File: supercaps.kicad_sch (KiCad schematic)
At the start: 17 parts, among them J7 XT30_F, J8 XT30_F, Q10 Q_PNP_BCE, Q9 Q_NPN_BCE, U17 TLV9301xDBV

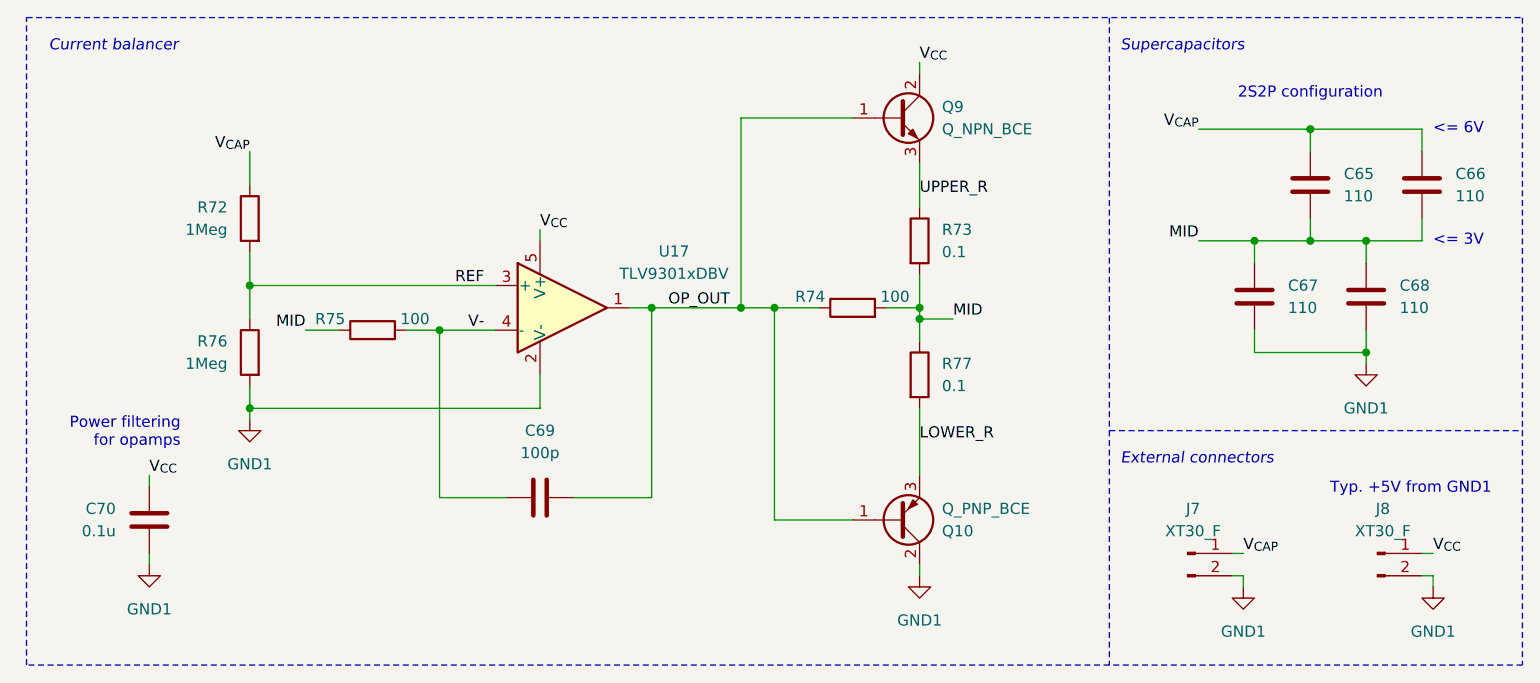
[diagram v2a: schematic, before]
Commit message: Selected BJTs for the supercap balancing circuitry
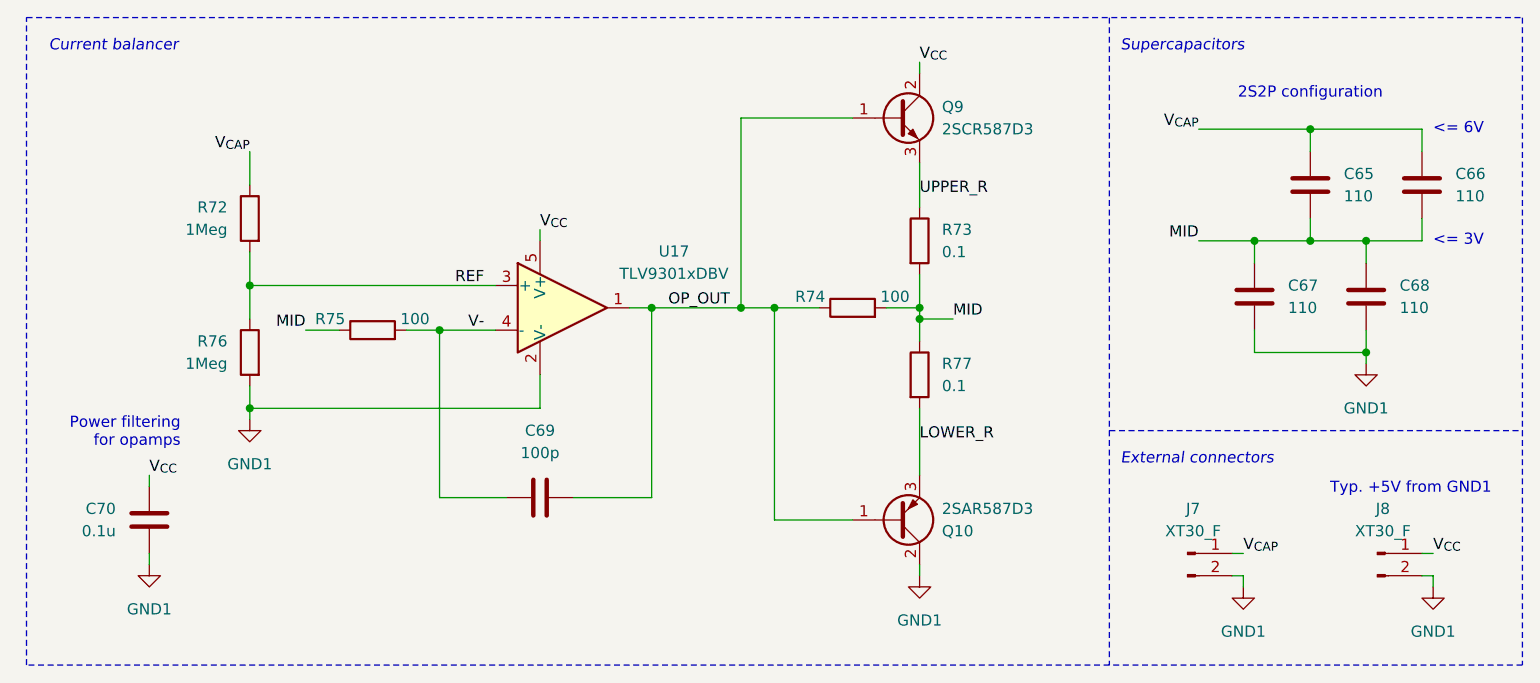
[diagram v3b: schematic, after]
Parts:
- Q10: value Q_PNP_BCE -> 2SAR587D3; footprint (none) -> Package_TO_SOT_SMD:TO-252-2; Mouser Part Number (none) -> 755-2SAR587D3FRATL
- Q9: value Q_NPN_BCE -> 2SCR587D3; footprint (none) -> Package_TO_SOT_SMD:TO-252-2; Mouser Part Number (none) -> 755-2SCR587D3FRATL
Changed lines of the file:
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@@
 			)
 		)
-		(property "Value" "Q_NPN_BCE"
+		(property "Value" "2SCR587D3"
 			(at 125.73 38.0999 0)
 			(effects
@@
 			)
 		)
-		(property "Footprint" ""
+		(property "Footprint" "Package_TO_SOT_SMD:TO-252-2"
 			(at 125.73 34.29 0)
 			(effects
@@
 			)
 		)
-		(property "Datasheet" "~"
+		(property "Datasheet" "https://fscdn.rohm.com/en/products/databook/datasheet/discrete/transistor/bipolar/2scr587d3fratl-e.pdf"
 			(at 120.65 36.83 0)
 			(effects
@@
 		)
 		(property "Description" "NPN transistor, base/collector/emitter"
+			(at 120.65 36.83 0)
+			(effects
+				(font
+					(size 1.27 1.27)
+				)
+				(hide yes)
+			)
+		)
+		(property "Mouser Part Number" "755-2SCR587D3FRATL"
 			(at 120.65 36.83 0)
 			(effects
@@
 			)
 		)
-		(property "Value" "Q_PNP_BCE"
+		(property "Value" "2SAR587D3"
 			(at 125.73 81.2801 0)
 			(effects
@@
 			)
 		)
-		(property "Footprint" ""
+		(property "Footprint" "Package_TO_SOT_SMD:TO-252-2"
 			(at 125.73 85.09 0)
 			(effects
@@
 			)
 		)
-		(property "Datasheet" "~"
+		(property "Datasheet" "https://fscdn.rohm.com/en/products/databook/datasheet/discrete/transistor/bipolar/2sar587d3fratl-e.pdf"
 			(at 120.65 82.55 0)
 			(effects
@@
 			(at 120.65 82.55 0)
 			(effects
+				(font
+					(size 1.27 1.27)
+				)
+				(hide yes)
+			)
+		)
+		(property "Mouser Part Number" "755-2SAR587D3FRATL"
+			(at 120.65 82.55 0)
+			(effects

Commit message: Adjusted some things + changed discharge to have a smaller time constant
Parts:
- R72, R76: Mouser Part Number (none) -> 603-RC0603FR-1010ML
- U17: Mouser Part Number (none) -> 595-TLV9301IDBVR
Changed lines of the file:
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@@
+			)
+		)
+		(property "Mouser Part Number" "595-TLV9301IDBVR"
+			(at 82.55 58.42 0)
+			(effects
+				(font
+					(size 1.27 1.27)
+				)
+				(hide yes)
 			)
 		)
@@
 			)
 		)
-		(property "Datasheet" "~"
+		(property "Datasheet" "https://www.mouser.com/datasheet/2/447/PYu_RC_Group_51_RoHS_L_11-1984063.pdf"
 			(at 46.99 48.26 0)
 			(effects
@@
 		)
 		(property "Description" "Resistor"
+			(at 46.99 48.26 0)
+			(effects
+				(font
+					(size 1.27 1.27)
+				)
+				(hide yes)
+			)
+		)
+		(property "Mouser Part Number" "603-RC0603FR-1010ML"
 			(at 46.99 48.26 0)
 			(effects
@@
 			)
 		)
-		(property "Datasheet" "~"
+		(property "Datasheet" "https://www.mouser.com/datasheet/2/447/PYu_RC_Group_51_RoHS_L_11-1984063.pdf"
 			(at 46.99 63.5 0)
 			(effects
@@
 			(at 46.99 63.5 0)
 			(effects
+				(font
+					(size 1.27 1.27)
+				)
+				(hide yes)
+			)
+		)
+		(property "Mouser Part Number" "603-RC0603FR-1010ML"
+			(at 46.99 63.5 0)
+			(effects

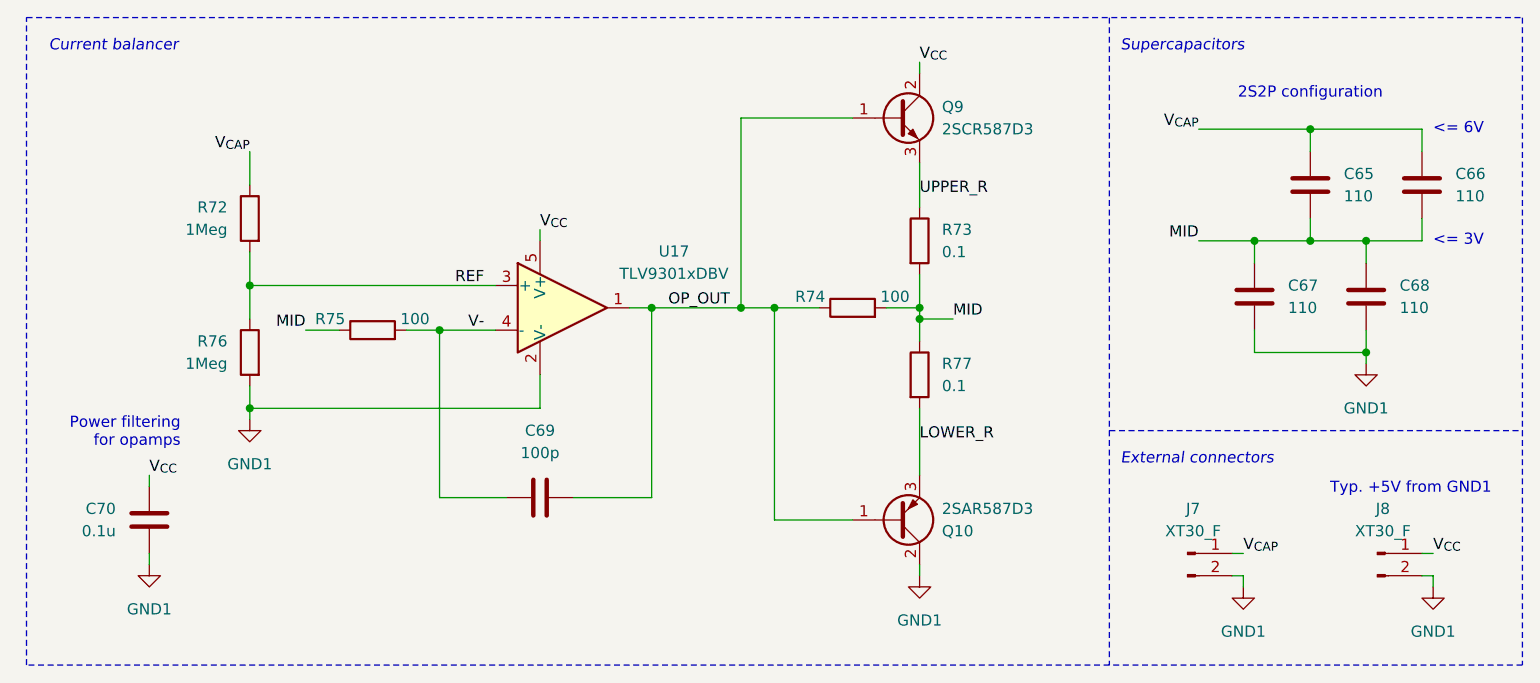
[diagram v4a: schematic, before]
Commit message: Renumbering components
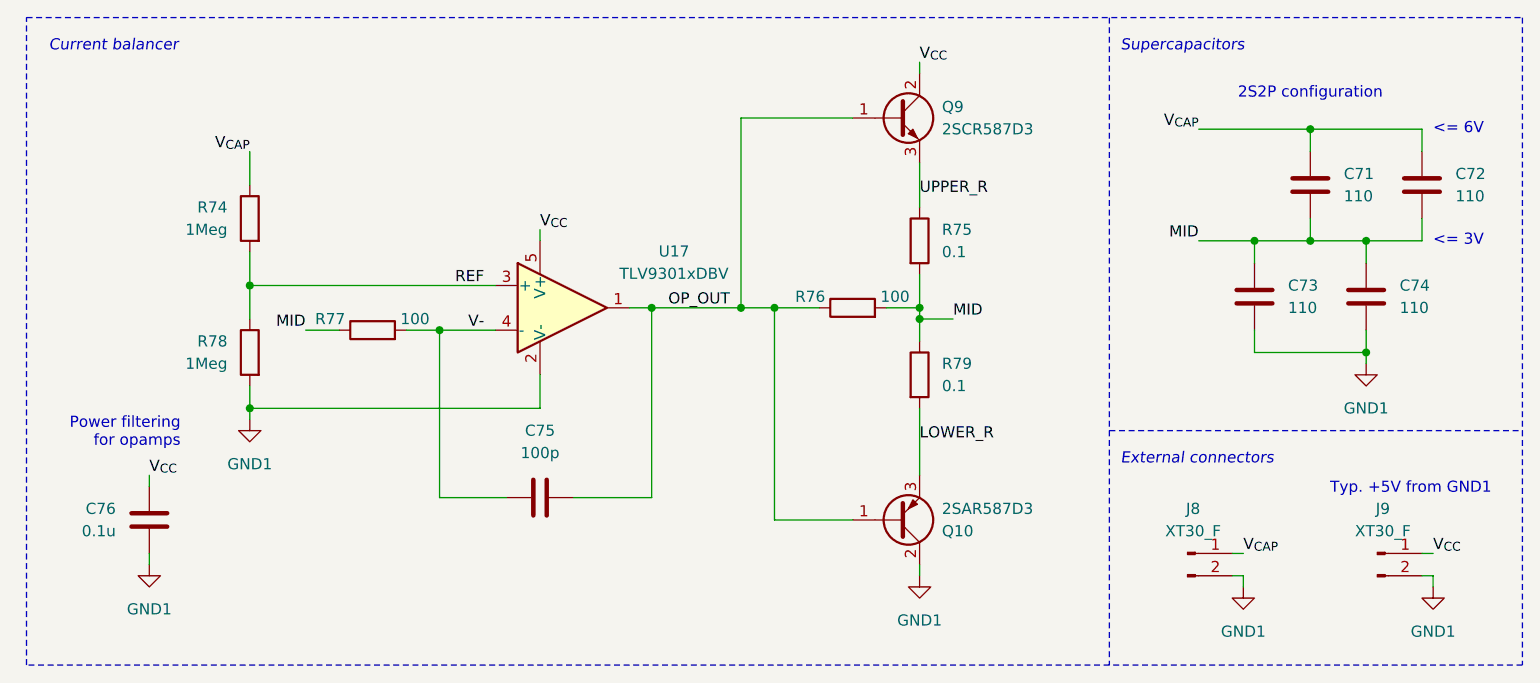
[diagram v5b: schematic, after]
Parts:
- renumbered C65 to C71, C66 to C72, C67 to C73, C68 to C74, C69 to C75, C70 to C76, J7 to J8, J8 to J9, R72 to R74, R73 to R75, R74 to R76, R75 to R77, R76 to R78, R77 to R79
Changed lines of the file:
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@@
 		(on_board yes)
 		(dnp no)
-		(property "Reference" "R77"
+		(property "Reference" "R79"
 			(at 125.73 64.7699 0)
 			(effects
@@
 			(project "SupercapManager"
 				(path "/6197145b-e7d4-44cc-9d90-537b6501bf60/e69614f9-5cd8-4aa3-ae42-53f80cb78886"
-					(reference "R77")
+					(reference "R79")
 					(unit 1)
 				)
@@
 		(dnp no)
 		(fields_autoplaced yes)
-		(property "Reference" "C69"
+		(property "Reference" "C75"
 			(at 80.01 72.39 90)
 			(effects
@@
 			(project ""
 				(path "/6197145b-e7d4-44cc-9d90-537b6501bf60/e69614f9-5cd8-4aa3-ae42-53f80cb78886"
-					(reference "C69")
+					(reference "C75")
 					(unit 1)
 				)
@@
 		(dnp no)
 		(fields_autoplaced yes)
-		(property "Reference" "C67"
+		(property "Reference" "C73"
 			(at 165.1 55.8799 0)
 			(effects
@@
 			(project "SupercapManager"
 				(path "/6197145b-e7d4-44cc-9d90-537b6501bf60/e69614f9-5cd8-4aa3-ae42-53f80cb78886"
-					(reference "C67")
+					(reference "C73")
 					(unit 1)
 				)
@@
 		(dnp no)
 		(fields_autoplaced yes)
-		(property "Reference" "#PWR099"
+		(property "Reference" "#PWR098"
 			(at 46.99 77.47 0)
 			(effects
@@
 			(project "SupercapManager"
 				(path "/6197145b-e7d4-44cc-9d90-537b6501bf60/e69614f9-5cd8-4aa3-ae42-53f80cb78886"
-					(reference "#PWR099")
+					(reference "#PWR098")
 					(unit 1)
 				)
@@
 		(dnp no)
 		(fields_autoplaced yes)
-		(property "Reference" "C70"
+		(property "Reference" "C76"
 			(at 31.75 81.2799 0)
 			(effects
@@
 			(project "SupercapManager"
 				(path "/6197145b-e7d4-44cc-9d90-537b6501bf60/e69614f9-5cd8-4aa3-ae42-53f80cb78886"
-					(reference "C70")
+					(reference "C76")
 					(unit 1)
 				)
@@
 		(dnp no)
 		(fields_autoplaced yes)
-		(property "Reference" "#PWR0102"
+		(property "Reference" "#PWR0101"
 			(at 160.02 96.52 0)
 			(effects
@@
 			(project ""
 				(path "/6197145b-e7d4-44cc-9d90-537b6501bf60/e69614f9-5cd8-4aa3-ae42-53f80cb78886"
-					(reference "#PWR0102")
+					(reference "#PWR0101")
 					(unit 1)
 				)
@@
 		(on_board yes)
 		(dnp no)
-		(property "Reference" "J8"
+		(property "Reference" "J9"
 			(at 175.895 81.28 0)
 			(effects
@@
 			(project "SupercapManager"
 				(path "/6197145b-e7d4-44cc-9d90-537b6501bf60/e69614f9-5cd8-4aa3-ae42-53f80cb78886"
-					(reference "J8")
+					(reference "J9")
 					(unit 1)
 				)
@@
 		(dnp no)
 		(fields_autoplaced yes)
-		(property "Reference" "#PWR098"
+		(property "Reference" "#PWR097"
 			(at 173.99 71.12 0)
 			(effects
@@
 			(project "SupercapManager"
 				(path "/6197145b-e7d4-44cc-9d90-537b6501bf60/e69614f9-5cd8-4aa3-ae42-53f80cb78886"
-					(reference "#PWR098")
+					(reference "#PWR097")
 					(unit 1)
 				)
@@
 		(on_board yes)
 		(dnp no)
-		(property "Reference" "R72"
+		(property "Reference" "R74"
 			(at 44.45 46.9899 0)
 			(effects
@@
 			(project ""
 				(path "/6197145b-e7d4-44cc-9d90-537b6501bf60/e69614f9-5cd8-4aa3-ae42-53f80cb78886"
-					(reference "R72")
+					(reference "R74")
 					(unit 1)
 				)
@@
 		(dnp no)
 		(fields_autoplaced yes)
-		(property "Reference" "C65"
+		(property "Reference" "C71"
 			(at 171.45 43.1799 0)
 			(effects
@@
 			(project "SupercapManager"
 				(path "/6197145b-e7d4-44cc-9d90-537b6501bf60/e69614f9-5cd8-4aa3-ae42-53f80cb78886"
-					(reference "C65")
+					(reference "C71")
 					(unit 1)
 				)
@@
 		(dnp no)
 		(fields_autoplaced yes)
-		(property "Reference" "#PWR0101"
+		(property "Reference" "#PWR0100"
 			(at 123.19 95.25 0)
 			(effects
@@
 			(project "SupercapManager"
 				(path "/6197145b-e7d4-44cc-9d90-537b6501bf60/e69614f9-5cd8-4aa3-ae42-53f80cb78886"
-					(reference "#PWR0101")
+					(reference "#PWR0100")
 					(unit 1)
 				)
@@
 		(on_board yes)
 		(dnp no)
-		(property "Reference" "J7"
+		(property "Reference" "J8"
 			(at 154.305 81.28 0)
 			(effects
@@
 			(project "SupercapManager"
 				(path "/6197145b-e7d4-44cc-9d90-537b6501bf60/e69614f9-5cd8-4aa3-ae42-53f80cb78886"
-					(reference "J7")
+					(reference "J8")
 					(unit 1)
 				)
@@
 		(dnp no)
 		(fields_autoplaced yes)
-		(property "Reference" "C66"
+		(property "Reference" "C72"
 			(at 184.15 43.1799 0)
 			(effects
@@
 			(project "SupercapManager"
 				(path "/6197145b-e7d4-44cc-9d90-537b6501bf60/e69614f9-5cd8-4aa3-ae42-53f80cb78886"
-					(reference "C66")
+					(reference "C72")
 					(unit 1)
 				)
@@
 		(on_board yes)
 		(dnp no)
-		(property "Reference" "R73"
+		(property "Reference" "R75"
 			(at 125.73 49.5299 0)
 			(effects
@@
 			(project "SupercapManager"
 				(path "/6197145b-e7d4-44cc-9d90-537b6501bf60/e69614f9-5cd8-4aa3-ae42-53f80cb78886"
-					(reference "R73")
+					(reference "R75")
 					(unit 1)
 				)
@@
 		(on_board yes)
 		(dnp no)
-		(property "Reference" "R76"
+		(property "Reference" "R78"
 			(at 44.45 62.2299 0)
 			(effects
@@
 			(project "SupercapManager"
 				(path "/6197145b-e7d4-44cc-9d90-537b6501bf60/e69614f9-5cd8-4aa3-ae42-53f80cb78886"
-					(reference "R76")
+					(reference "R78")
 					(unit 1)
 				)
@@
 		(on_board yes)
 		(dnp no)
-		(property "Reference" "R75"
+		(property "Reference" "R77"
 			(at 56.134 59.69 90)
 			(effects
@@
 			(project ""
 				(path "/6197145b-e7d4-44cc-9d90-537b6501bf60/e69614f9-5cd8-4aa3-ae42-53f80cb78886"
-					(reference "R75")
+					(reference "R77")
 					(unit 1)
 				)
@@
 		(dnp no)
 		(fields_autoplaced yes)
-		(property "Reference" "#PWR0100"
+		(property "Reference" "#PWR099"
 			(at 35.56 93.98 0)
 			(effects
@@
 			(project "SupercapManager"
 				(path "/6197145b-e7d4-44cc-9d90-537b6501bf60/e69614f9-5cd8-4aa3-ae42-53f80cb78886"
-					(reference "#PWR0100")
+					(reference "#PWR099")
 					(unit 1)
 				)
@@
 		(dnp no)
 		(fields_autoplaced yes)
-		(property "Reference" "#PWR0103"
+		(property "Reference" "#PWR0102"
 			(at 181.61 96.52 0)
 			(effects
@@
 			(project "SupercapManager"
 				(path "/6197145b-e7d4-44cc-9d90-537b6501bf60/e69614f9-5cd8-4aa3-ae42-53f80cb78886"
-					(reference "#PWR0103")
+					(reference "#PWR0102")
 					(unit 1)
 				)
@@
 		(on_board yes)
 		(dnp no)
-		(property "Reference" "R74"
+		(property "Reference" "R76"
 			(at 110.744 57.15 90)
 			(effects
@@
 			(project "SupercapManager"
 				(path "/6197145b-e7d4-44cc-9d90-537b6501bf60/e69614f9-5cd8-4aa3-ae42-53f80cb78886"
-					(reference "R74")
+					(reference "R76")
 					(unit 1)
 				)
@@
 		(dnp no)
 		(fields_autoplaced yes)
-		(property "Reference" "C68"
+		(property "Reference" "C74"
 			(at 177.8 55.8799 0)
 			(effects
@@
 			(project "SupercapManager"
 				(path "/6197145b-e7d4-44cc-9d90-537b6501bf60/e69614f9-5cd8-4aa3-ae42-53f80cb78886"
-					(reference "C68")
-					(unit 1)
-				)
+					(reference "C74")
+					(unit 1)
+				)

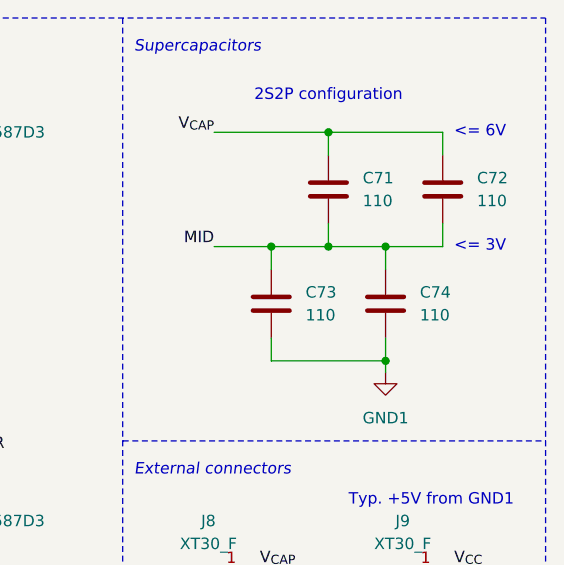
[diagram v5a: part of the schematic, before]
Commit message: Add voltage ratings to capacitors & respec caps to not explode
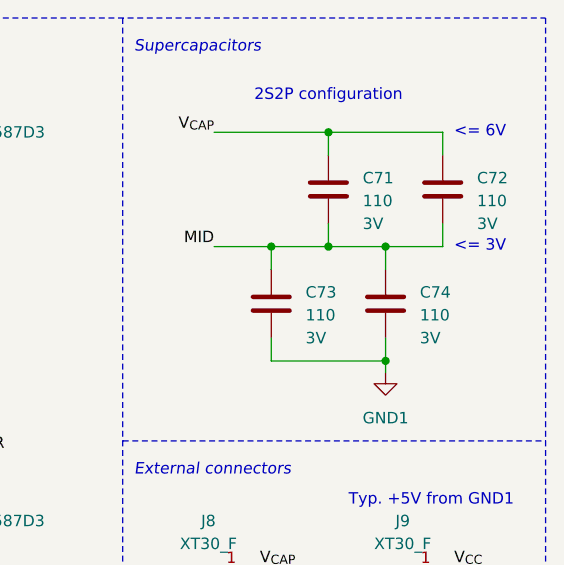
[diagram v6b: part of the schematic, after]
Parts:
- C71, C72, C73, C74: Voltage Rating (none) -> 3V
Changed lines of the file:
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@@
 		(on_board no)
 		(dnp no)
-		(fields_autoplaced yes)
 		(property "Reference" "C73"
 			(at 165.1 55.8799 0)
@@
 				)
 				(hide yes)
+			)
+		)
+		(property "Voltage Rating" "3V"
+			(at 165.1 60.96 0)
+			(effects
+				(font
+					(size 1.27 1.27)
+				)
+				(justify left)
 			)
 		)
@@
 		(on_board no)
 		(dnp no)
-		(fields_autoplaced yes)
 		(property "Reference" "C71"
 			(at 171.45 43.1799 0)
@@
 				)
 				(hide yes)
+			)
+		)
+		(property "Voltage Rating" "3V"
+			(at 171.45 48.26 0)
+			(effects
+				(font
+					(size 1.27 1.27)
+				)
+				(justify left)
 			)
 		)
@@
 		(on_board no)
 		(dnp no)
-		(fields_autoplaced yes)
 		(property "Reference" "C72"
 			(at 184.15 43.1799 0)
@@
 				)
 				(hide yes)
+			)
+		)
+		(property "Voltage Rating" "3V"
+			(at 184.15 48.26 0)
+			(effects
+				(font
+					(size 1.27 1.27)
+				)
+				(justify left)
 			)
 		)
@@
 		(on_board no)
 		(dnp no)
-		(fields_autoplaced yes)
 		(property "Reference" "C74"
 			(at 177.8 55.8799 0)
@@
 			)
 		)
+		(property "Voltage Rating" "3V"
+			(at 177.8 60.96 0)
+			(effects
+				(font
+					(size 1.27 1.27)
+				)
+				(justify left)
+			)
+		)

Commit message: Sourcing various parts
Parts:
- R75, R79: footprint Resistor_SMD:R_0603_1608Metric_Pad0.98x0.95mm_HandSolder -> Resistor_SMD:R_1206_3216Metric_Pad1.30x1.75mm_HandSolder; Mouser Part Number (none) -> 504-MFHA1206R1000FC
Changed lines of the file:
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@@
 			)
 		)
-		(property "Footprint" "Resistor_SMD:R_0603_1608Metric_Pad0.98x0.95mm_HandSolder"
+		(property "Footprint" "Resistor_SMD:R_1206_3216Metric_Pad1.30x1.75mm_HandSolder"
 			(at 121.412 66.04 90)
 			(effects
@@
 			)
 		)
-		(property "Datasheet" "~"
+		(property "Datasheet" "https://www.eaton.com/content/dam/eaton/products/electronic-components/resources/data-sheet/eaton-mfha-automotive-smd-current-sense-resistor-metal-film-data-sheet-elx1178.pdf"
 			(at 123.19 66.04 0)
 			(effects
@@
 		)
 		(property "Description" "Resistor"
+			(at 123.19 66.04 0)
+			(effects
+				(font
+					(size 1.27 1.27)
+				)
+				(hide yes)
+			)
+		)
+		(property "Mouser Part Number" "504-MFHA1206R1000FC"
 			(at 123.19 66.04 0)
 			(effects
@@
 			)
 		)
-		(property "Footprint" "Resistor_SMD:R_0603_1608Metric_Pad0.98x0.95mm_HandSolder"
+		(property "Footprint" "Resistor_SMD:R_1206_3216Metric_Pad1.30x1.75mm_HandSolder"
 			(at 121.412 50.8 90)
 			(effects
@@
 			)
 		)
-		(property "Datasheet" "~"
+		(property "Datasheet" "https://www.eaton.com/content/dam/eaton/products/electronic-components/resources/data-sheet/eaton-mfha-automotive-smd-current-sense-resistor-metal-film-data-sheet-elx1178.pdf"
 			(at 123.19 50.8 0)
 			(effects
@@
 			(at 123.19 50.8 0)
 			(effects
+				(font
+					(size 1.27 1.27)
+				)
+				(hide yes)
+			)
+		)
+		(property "Mouser Part Number" "504-MFHA1206R1000FC"
+			(at 123.19 50.8 0)
+			(effects
